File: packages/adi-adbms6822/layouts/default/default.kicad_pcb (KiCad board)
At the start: 2 copper layers, 15 parts

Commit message: push for initial release
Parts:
- R3: value 20kΩ ±1% 62.5mW -> 10Ω ±1% 62.5mW; footprint UNI_ROYAL_0402WGF2002TCE:R0402 -> UNI_ROYAL_0402WGF100JTCE:R0402
- R8: value 18kΩ ±1% 62.5mW -> 0Ω 62.5mW; footprint UNI_ROYAL_0402WGF1802TCE:R0402 -> UNI_ROYAL_0402WGF0000TCE:R0402
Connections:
- R2 pad 2: -hv-0 -> gnd
- R3 pad 2: gnd -> -hv-0

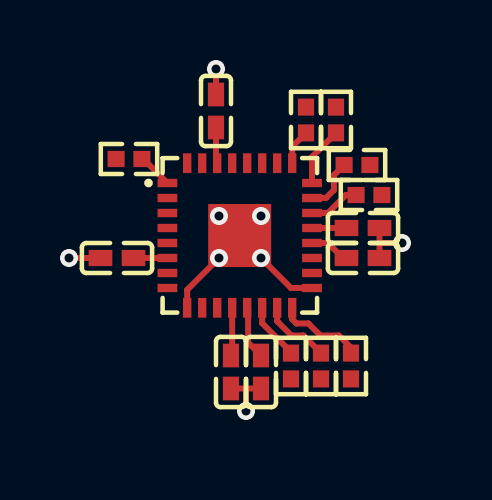
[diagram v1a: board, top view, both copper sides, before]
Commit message: Feature: Build ADI adbms6830 (#100)
* gbfo layout complete

* add dac

* minor layout tweak

* halfway thru usage layout

* almost ready for release

* built on jlc

---------

Co-authored-by: Narayan Powderly <narayan@atopile.io>
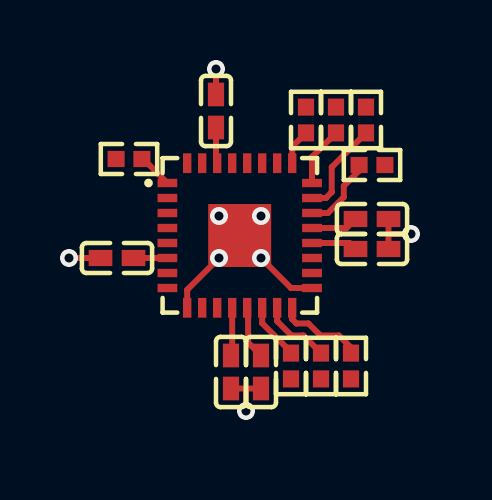
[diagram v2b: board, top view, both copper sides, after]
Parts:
- moved R8 1.53 mm to (164.4, 95.8), turned to 90 degrees
- moved R4 1.00 mm to (164.6, 97.3)
- moved C4 0.42 mm to (164.6, 100.1)
- moved C5 0.42 mm to (164.6, 99.1)
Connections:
- net -hv-0 renamed vdds_spi_power-VCC
- net -hv-1 renamed vdd_iso_spi_power-VCC
- net IM renamed IM_N
- net IM2 renamed IM2_N
- net IP renamed IP_P
- net IP2 renamed IP2_P
- net PICO renamed spi[0]-MOSI
- net PICO2 renamed spi[1]-MOSI
- net POCI renamed spi[0]-MISO
- net POCI2 renamed spi[1]-MISO
- net SCK renamed spi[0]-SCLK
- net SCK2 renamed spi[1]-SCLK
- net VP renamed vp_power-VCC
- net gnd renamed GND
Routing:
- net RTO_2_CONFIG: track 1.81 -> 3.19 mm
- net PHAPOL_2_CONFIG: track 1.72 -> 2.56 mm

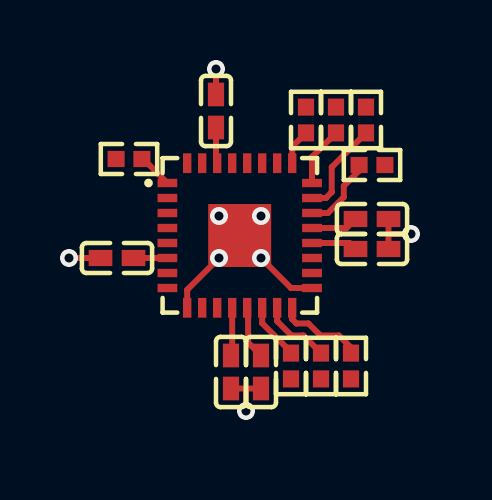
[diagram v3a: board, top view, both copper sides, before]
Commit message: adbms68xx: Bringup Fixes (#164)
* update mode to MASTER for 6822

* connect switch to power

* update termination resistors

* fix connector flipped issue, updated termination

* add adcs and remove gpio connections

* bump version

* bump version

* layout tidy up

* frozen build passing on 6830

* remove claude and github litter

* remove windsurf litter

---------

Co-authored-by: Nicholas Krstevski <nick@atopile.io>
Co-authored-by: Nick Krstevski <51719418+nickkrstevski@users.noreply.github.com>
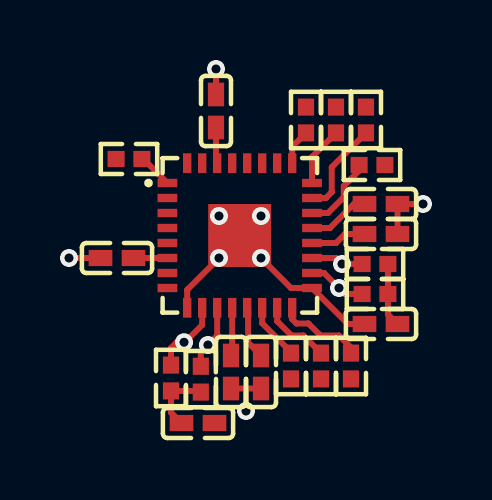
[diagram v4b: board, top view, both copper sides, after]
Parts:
- added C7: 100nF ±10% 16V X7R, Samsung_Electro_Mechanics_CL05B104KO5NNNC:C0402, F.Cu at (158.8, 105.9)
- added C8: 100nF ±10% 16V X7R, Samsung_Electro_Mechanics_CL05B104KO5NNNC:C0402, F.Cu at (164.9, 102.6)
- added R10: 49.9Ω ±1% 62.5mW, YAGEO_RC0402FR_0749R9L:R0402, F.Cu at (157.9, 104.4)
- added R11: 49.9Ω ±1% 62.5mW, YAGEO_RC0402FR_0749R9L:R0402, F.Cu at (164.7, 100.6)
- added R12: 49.9Ω ±1% 62.5mW, YAGEO_RC0402FR_0749R9L:R0402, F.Cu at (164.7, 101.6)
- added R9: 49.9Ω ±1% 62.5mW, YAGEO_RC0402FR_0749R9L:R0402, F.Cu at (158.9, 104.4)
- moved C4 0.58 mm to (164.9, 99.6)
- moved C5 0.58 mm to (164.9, 98.6)
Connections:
- R1 pad 2: GND -> vdds_spi_power-VCC
- R2 pad 2: GND -> vdds_spi_power-VCC
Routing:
- net IM_N: track 0.00 -> 2.50 mm, vias 0 -> 1
- net GND: track 9.61 -> 12.0 mm
- net iso_1_termination_midpoint: track 0.00 -> 2.23 mm
- net IP_P: track 0.00 -> 2.17 mm, vias 0 -> 1
- net iso_2_termination_midpoint: track 0.00 -> 2.13 mm
- net IM2_N: track 0.00 -> 1.96 mm, vias 0 -> 1
- net IP2_P: track 0.00 -> 1.75 mm, vias 0 -> 1
- net vp_power-VCC: track 3.35 -> 3.86 mm

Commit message: update adbms parts
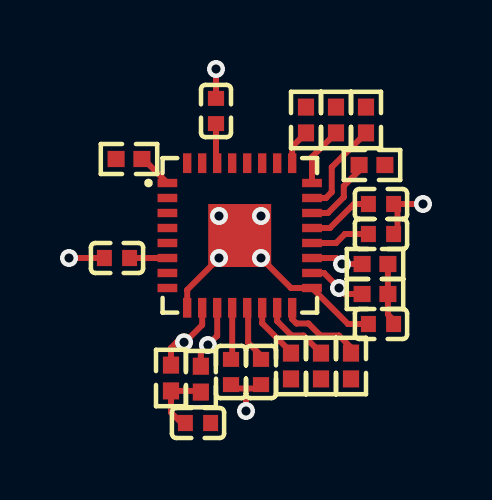
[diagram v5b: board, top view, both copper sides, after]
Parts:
- C1, C2, C3, C4, C5, C6: value 1µF ±10% 25V X5R -> 1e-06F
- C7, C8: value 100nF ±10% 16V X7R -> 1.0000000000000001e-07F
- R1, R2: value 10kΩ ±1% 62.5mW -> 10000.0Ω
- R10, R11, R12, R9: value 49.9Ω ±1% 62.5mW -> 49.9Ω
- R3, R4, R5, R6: value 10Ω ±1% 62.5mW -> 10.0Ω
- R7, R8: value 0Ω 62.5mW -> 10.0Ω
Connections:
- net GND renamed lv
- net IM2_N renamed 18_N
- net INTR2 renamed 31
- net IP2_P renamed 19_P
- net WAKE2 renamed 32
- net iso_1_termination_midpoint renamed isoSPI_dc_bias_caps[0]-power-hv
- net iso_2_termination_midpoint renamed isoSPI_dc_bias_caps[1]-power-hv
- net nCS2 renamed 29
- net spi[0]-MISO renamed POCI
- net spi[0]-MOSI renamed PICO
- net spi[0]-SCLK renamed SCK
- net spi[1]-MISO renamed 27
- net spi[1]-MOSI renamed 26
- net spi[1]-SCLK renamed 28
- net vdd_iso_spi_power-VCC renamed bypass_capacitors[3]-power-hv
- net vdds_spi_power-VCC renamed bypass_capacitors[1]-power-hv
- net vp_power-VCC renamed bypass_capacitors[5]-power-hv

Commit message: review tool updates
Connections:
- net 26 renamed spi[1]-MOSI
- net 27 renamed spi[1]-MISO
- net 28 renamed spi[1]-SCLK
- net PICO renamed spi[0]-MOSI
- net POCI renamed spi[0]-MISO
- net SCK renamed spi[0]-SCLK
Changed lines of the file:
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@@
 			(usegerberadvancedattributes yes)
 			(creategerberjobfile yes)
-			(dashed_line_dash_ratio 12.000000)
-			(dashed_line_gap_ratio 3.000000)
+			(dashed_line_dash_ratio 12)
+			(dashed_line_gap_ratio 3)
 			(svgprecision 4)
 			(plotframeref no)
@@
 			(hpglpennumber 1)
 			(hpglpenspeed 20)
-			(hpglpendiameter 15.000000)
+			(hpglpendiameter 15)
 			(pdf_front_fp_property_popups yes)
 			(pdf_back_fp_property_popups yes)
@@
 	(net 0 "")
 	(net 1 "RTO_1_CONFIG")
-	(net 2 "SCK")
+	(net 2 "spi[0]-SCLK")
 	(net 3 "bypass_capacitors[5]-power-hv")
 	(net 4 "RTO_2_CONFIG")
 	(net 5 "32")
 	(net 6 "PHAPOL_2_CONFIG")
-	(net 7 "POCI")
+	(net 7 "spi[0]-MISO")
 	(net 8 "MSTR_1_CONFIG")
 	(net 9 "WAKE")
 	(net 10 "bypass_capacitors[3]-power-hv")
 	(net 11 "MSTR_2_CONFIG")
-	(net 12 "27")
+	(net 12 "spi[1]-MISO")
 	(net 13 "XCVRMD_1_CONFIG")
-	(net 14 "PICO")
-	(net 15 "28")
+	(net 14 "spi[0]-MOSI")
+	(net 15 "spi[1]-SCLK")
 	(net 16 "PHAPOL_1_CONFIG")
 	(net 17 "nCS")
-	(net 18 "26")
+	(net 18 "spi[1]-MOSI")
 	(net 19 "INTR")
 	(net 20 "29")
@@
 			(size 0.66 0.28)
 			(layers "F.Cu" "F.Paste" "F.Mask")
-			(net 14 "PICO")
+			(net 14 "spi[0]-MOSI")
 		)
 		(pad "3" smd rect
@@
 			(size 0.66 0.28)
 			(layers "F.Cu" "F.Paste" "F.Mask")
-			(net 7 "POCI")
+			(net 7 "spi[0]-MISO")
 		)
 		(pad "4" smd rect
@@
 			(size 0.66 0.28)
 			(layers "F.Cu" "F.Paste" "F.Mask")
-			(net 2 "SCK")
+			(net 2 "spi[0]-SCLK")
 		)
 		(pad "5" smd rect
@@
 			(size 0.28 0.66)
 			(layers "F.Cu" "F.Paste" "F.Mask")
-			(net 18 "26")
+			(net 18 "spi[1]-MOSI")
 		)
 		(pad "27" smd rect
@@
 			(size 0.28 0.66)
 			(layers "F.Cu" "F.Paste" "F.Mask")
-			(net 12 "27")
+			(net 12 "spi[1]-MISO")
 		)
 		(pad "28" smd rect
@@
 			(size 0.28 0.66)
 			(layers "F.Cu" "F.Paste" "F.Mask")
-			(net 15 "28")
+			(net 15 "spi[1]-SCLK")
 		)
 		(pad "29" smd rect

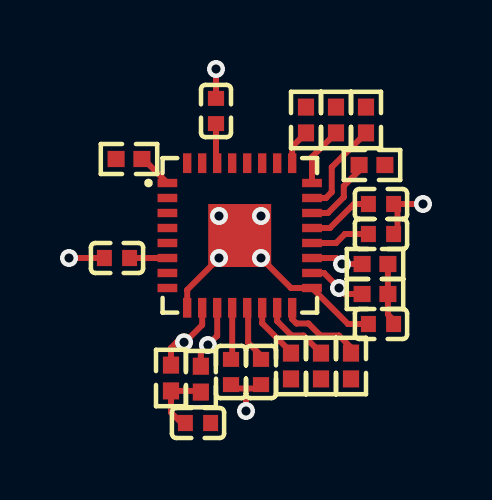
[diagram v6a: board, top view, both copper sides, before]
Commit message: remove all those other changes, just bosch baby
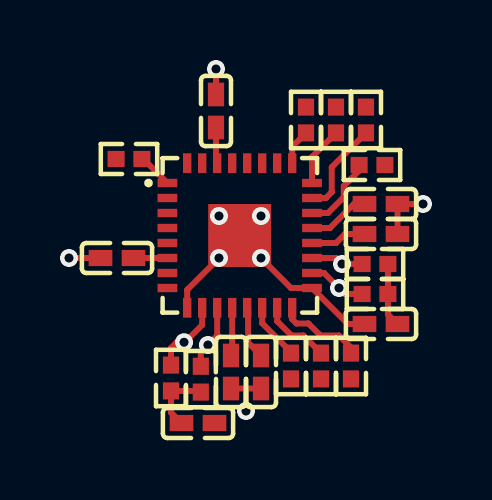
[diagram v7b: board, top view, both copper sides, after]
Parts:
- C1, C2, C3, C4, C5, C6: value 1e-06F -> 1µF ±10% 25V X5R
- C7, C8: value 1.0000000000000001e-07F -> 100nF ±10% 16V X7R
- R1, R2: value 10000.0Ω -> 10kΩ ±1% 62.5mW
- R10, R11, R12, R9: value 49.9Ω -> 49.9Ω ±1% 62.5mW
- R3, R4, R5, R6: value 10.0Ω -> 10Ω ±1% 62.5mW
- R7, R8: value 10.0Ω -> 0Ω 62.5mW
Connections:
- net 18_N renamed IM2_N
- net 19_P renamed IP2_P
- net 29 renamed nCS2
- net 31 renamed INTR2
- net 32 renamed WAKE2
- net bypass_capacitors[1]-power-hv renamed vdds_spi_power-VCC
- net bypass_capacitors[3]-power-hv renamed vdd_iso_spi_power-VCC
- net bypass_capacitors[5]-power-hv renamed vp_power-VCC
- net isoSPI_dc_bias_caps[0]-power-hv renamed iso_1_termination_midpoint
- net isoSPI_dc_bias_caps[1]-power-hv renamed iso_2_termination_midpoint
- net lv renamed GND
